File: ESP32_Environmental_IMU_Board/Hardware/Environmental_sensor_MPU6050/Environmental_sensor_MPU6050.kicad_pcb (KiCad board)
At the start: 4 copper layers, 0 parts

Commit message: PCB layout started
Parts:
- added BT1: CH291-1220LF, CH291-1220LF:BAT_CH291-1220LF, F.Cu at (142.9, 93.1)
- added C1: 10uF, Capacitor_SMD:C_0805_2012Metric, F.Cu at (130.3, 65.7)
- added C10: 0.1uF, Capacitor_SMD:C_0603_1608Metric, F.Cu at (123.9, 57.3)
- added C11: 0.1uF, Capacitor_SMD:C_0603_1608Metric, F.Cu at (143.4, 63.6)
- added C12: 1uF, Capacitor_SMD:C_0603_1608Metric, F.Cu at (130.6, 59.3)
- added C13: 10uF, Capacitor_SMD:C_0805_2012Metric, F.Cu at (136.2, 70.3)
- added C14: 0.1uF, Capacitor_SMD:C_0603_1608Metric, F.Cu at (136.0, 68.5)
- added C15: 1uF, Capacitor_SMD:C_0603_1608Metric, F.Cu at (145.0, 81.0)
- added C16: 0.1uF, Capacitor_SMD:C_0603_1608Metric, F.Cu at (144.9, 79.5)
- added C17: 0.1uF, Capacitor_SMD:C_0603_1608Metric, F.Cu at (141.0, 77.0)
- added C2: 0.1uF, Capacitor_SMD:C_0603_1608Metric, F.Cu at (132.1, 65.5)
- added C4: 10uF, Capacitor_SMD:C_0805_2012Metric, F.Cu at (138.1, 65.4)
- added C7: 0.1uF, Capacitor_SMD:C_0603_1608Metric, F.Cu at (139.9, 65.2)
- added C8: 10uF, Capacitor_SMD:C_0805_2012Metric, F.Cu at (145.2, 63.7)
- added C9: 0.1uF, Capacitor_SMD:C_0603_1608Metric, F.Cu at (130.6, 56.2)
- added D1: MBR0520, Diode_SMD:D_SOD-123, F.Cu at (126.8, 65.3)
- added D2: RED_LED, LED_SMD:LED_0201_0603Metric, F.Cu at (133.6, 62.0)
- added D3: RED_LED, LED_SMD:LED_0201_0603Metric, F.Cu at (145.3, 66.7)
- added D4: RED_LED, LED_SMD:LED_0201_0603Metric, F.Cu at (142.0, 67.4)
- added D5: RED_LED, LED_SMD:LED_0201_0603Metric, F.Cu at (145.3, 69.5)
- added FID1: Fiducial, Fiducial:Fiducial_0.75mm_Mask1.5mm, F.Cu at (166.7, 102.7)
- added FID2: Fiducial, Fiducial:Fiducial_0.75mm_Mask1.5mm, F.Cu at (119.8, 56.9)
- added FID3: Fiducial, Fiducial:Fiducial_0.75mm_Mask1.5mm, F.Cu at (120.4, 102.3)
- added J1: Conn_01x04_Pin, Connector_PinHeader_2.54mm:PinHeader_1x04_P2.54mm_Vertical, F.Cu at (168.4, 91.8)
- added J2: Conn_01x04_Pin, Connector_PinHeader_2.54mm:PinHeader_1x04_P2.54mm_Vertical, F.Cu at (124.0, 98.8)
- added J3: USB_C_Receptacle_USB2.0_16P, Connector_USB:USB_C_Receptacle_HCTL_HC-TYPE-C-16P-01A, F.Cu at (119.5, 69.4)
- added J4: Micro_SD_Card, Connector_Card:microSD_HC_Hirose_DM3AT-SF-PEJM5, F.Cu at (126.3, 82.9)
- added R1: 4.7k, Resistor_SMD:R_0603_1608Metric, F.Cu at (164.7, 85.3)
- added R10: 1K, Resistor_SMD:R_0603_1608Metric, F.Cu at (147.6, 69.9)
- added R11: 22, Resistor_SMD:R_0603_1608Metric, F.Cu at (132.6, 69.0)
- added R12: 22, Resistor_SMD:R_0603_1608Metric, F.Cu at (132.6, 70.5)
- added R13: 33, Resistor_SMD:R_0603_1608Metric, F.Cu at (136.7, 83.4)
- added R14: 33, Resistor_SMD:R_0603_1608Metric, F.Cu at (136.7, 79.0)
- added R15: 0, Resistor_SMD:R_0603_1608Metric, F.Cu at (136.7, 77.0)
- added R16: 10k, Resistor_SMD:R_0603_1608Metric, F.Cu at (142.6, 77.0)
- added R17: 33, Resistor_SMD:R_0603_1608Metric, F.Cu at (136.7, 81.2)
- added R2: 4.7k, Resistor_SMD:R_0603_1608Metric, F.Cu at (164.7, 82.8)
- added R3: 0, Resistor_SMD:R_0603_1608Metric, F.Cu at (147.7, 62.7)
- added R4: 10k, Resistor_SMD:R_0603_1608Metric, F.Cu at (147.7, 64.3)
- added R5: 5.1k, Resistor_SMD:R_0603_1608Metric, F.Cu at (125.9, 68.1)
- added R6: 5.1k, Resistor_SMD:R_0603_1608Metric, F.Cu at (125.9, 71.1)
- added R7: 1K, Resistor_SMD:R_0603_1608Metric, F.Cu at (129.8, 61.6)
- added R8: 1K, Resistor_SMD:R_0603_1608Metric, F.Cu at (147.7, 67.1)
- added R9: 1K, Resistor_SMD:R_0603_1608Metric, F.Cu at (142.7, 66.1)
- added SW1: SW_Push, Button_Switch_SMD:SW_Push_SPST_NO_Alps_SKRK, F.Cu at (133.2, 57.5)
- added SW2: SW_Push, Button_Switch_SMD:SW_Push_SPST_NO_Alps_SKRK, F.Cu at (126.4, 57.5)
- added TP3: TP_GND, Test Point:TestPoint_Pad_D2.5mm, F.Cu at (124.6, 93.5)
- added TP6: TP_3V3, Test Point:TestPoint_Pad_D2.5mm, F.Cu at (128.8, 93.5)
- added TP7: TP_TX, Test Point:TestPoint_Pad_D2.5mm, F.Cu at (157.9, 97.1)
- added TP8: TP_RX, Test Point:TestPoint_Pad_D2.5mm, F.Cu at (161.7, 97.0)
- added U2: AP2112K-3.3, Package_TO_SOT_SMD:SOT-23-5, F.Cu at (135.0, 65.5)
- added U3: USBLC6-2P6, Package_TO_SOT_SMD:SOT-666, F.Cu at (129.5, 69.6)
- added U4: ESP32-S3-WROOM-1, RF_Module:ESP32-S3-WROOM-1, F.Cu at (159.0, 66.7)
- added U5: BME280, Package_LGA:Bosch_LGA-8_2.5x2.5mm_P0.65mm_ClockwisePinNumbering, F.Cu at (144.9, 77.1)
- added U6: DS3231M, Package_SO:SOIC-16W_7.5x10.3mm_P1.27mm, F.Cu at (156.9, 87.3)
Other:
- board outline added: 53.5 x 52.1 mm

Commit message: PCB layout started
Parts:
- added C1: 0.1uF, Capacitor_SMD:C_0805_2012Metric, F.Cu at (71.8, 42.4)
- added C12: 100nF, Capacitor_SMD:C_0805_2012Metric, F.Cu at (76.2, 42.4)
- added C13: 22uF/6.3V, Capacitor_SMD:C_0805_2012Metric, F.Cu at (76.2, 45.4)
- added C2: NS, Capacitor_SMD:C_0805_2012Metric, F.Cu at (71.8, 45.4)
- added C22: 100nF, Capacitor_SMD:C_0805_2012Metric, F.Cu at (76.2, 48.4)
- added C23: 100nF, Capacitor_SMD:C_0805_2012Metric, F.Cu at (76.2, 51.4)
- added C24: 1uF, Capacitor_SMD:C_0603_1608Metric, F.Cu at (89.0, 46.7)
- added C25: 0.1uF, Capacitor_SMD:C_0603_1608Metric, F.Cu at (89.0, 49.2)
- added C3: 10uF/50V, Capacitor_SMD:C_0805_2012Metric, F.Cu at (71.8, 48.4)
- added C5: 220pF, Capacitor_SMD:C_0805_2012Metric, F.Cu at (71.8, 51.4)
- added C8: 4.7uF, Capacitor_SMD:C_0805_2012Metric, F.Cu at (71.8, 54.4)
- added CIN1: 10uF, Capacitor_SMD:C_0805_2012Metric, F.Cu at (76.2, 54.4)
- added D2: RED_LED, LED_SMD:LED_0201_0603Metric, F.Cu at (99.5, 36.5)
- added D3: D_Schottky, Diode_SMD:D_SMA, F.Cu at (91.1, 43.1)
- added D4: D, Diode_SMD:D_SOD-123F, F.Cu at (97.8, 53.1)
- added D5: D, Diode_SMD:D_SOD-123F, F.Cu at (97.8, 56.5)
- added IC1: MP1584EN-LF-Z, MP1584EN-LF-Z:SOIC127P600X170-9N, F.Cu at (82.7, 52.7)
- added J2: Conn_01x02, Connector_JST:JST_PH_B2B-PH-K_1x02_P2.00mm_Vertical, F.Cu at (95.9, 31.8)
- added L1: 10uH, Inductor_SMD:L_6.3x6.3_H3, F.Cu at (82.7, 44.8)
- added R12: 4.7k, Resistor_SMD:R_0603_1608Metric, F.Cu at (93.0, 49.2)
- added R13: 4.7k, Resistor_SMD:R_0603_1608Metric, F.Cu at (93.0, 51.7)
- added R5: 200k, Resistor_SMD:R_0603_1608Metric, F.Cu at (89.0, 56.7)
- added R8: 40k, Resistor_SMD:R_0603_1608Metric, F.Cu at (89.0, 59.2)
- added R9: 124k, Resistor_SMD:R_0603_1608Metric, F.Cu at (93.0, 46.7)
- added R_LED1: 1K, Resistor_SMD:R_0603_1608Metric, F.Cu at (93.0, 54.2)
- added R_PRG1: 1K, Resistor_SMD:R_0603_1608Metric, F.Cu at (93.0, 56.7)
- added U1: MCP73831-2-OT, Package_TO_SOT_SMD:SOT-23-5, F.Cu at (95.5, 38.0)
- added U10: MLX90614ESF-BAA-000-TU, MLX90614ESF-BAA-000-TU:TO254P942H425-4, F.Cu at (87.6, 34.4)
- added U6: SCD40-D-R2, Sensor:Sensirion_SCD4x-1EP_10.1x10.1mm_P1.25mm_EP4.8x4.8mm, F.Cu at (75.8, 35.0)
- added U8: ENS160-BGLM, ENS160-BGLM:XDCR_ENS160-BGLM, F.Cu at (98.0, 48.4)
- added U9: OPT3001IDNPRQ1, OPT3001IDNPRQ1:SON65P200X200X65-7N, F.Cu at (97.7, 42.6)
- R1: value 4.7k -> 68.1k
- R2: value 4.7k -> 100k
- moved R1 82.9 mm to (89.0, 51.7), turned to 0 degrees
- moved R2 81.0 mm to (89.0, 54.2), turned to 0 degrees
- renumbered C4 to C10, C7 to C11, C8 to C14, C11 to C15, C9 to C16, C10 to C17, C12 to C18, C15 to C19, C16 to C20, C17 to C21, C1 to C4, C2 to C6, C13 to C7, C14 to C9, D2 to D6, D3 to D7, D4 to D8, D5 to D9, J3 to J1, J2 to J3, J1 to J4, J4 to J5, R3 to R10, R4 to R11, R16 to R14, R13 to R15, R17 to R16, R14 to R17, R15 to R18, R5 to R3, R6 to R4, R11 to R6, R12 to R7, R7 to R_LED2, R8 to R_LED3, R9 to R_LED4, R10 to R_LED5, TP3 to TP1, TP6 to TP2, TP7 to TP3, TP8 to TP4, U5 to U4, U4 to U5, U6 to U7
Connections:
- J4 pad 3: Net-(J1-Pin_3) -> SCL/IO9
- J4 pad 4: Net-(J1-Pin_4) -> SDA/IO8
- R1 pad 1: Net-(J1-Pin_3) -> GND
- R1 pad 2: SCL/IO9 -> Net-(C5-Pad2)
- R10 pad 2: ESP32_3V3 -> Net-(D5-A)
- R2 pad 1: Net-(J1-Pin_4) -> BAT+
- R2 pad 2: SDA/IO8 -> BAT+
- TP2 pad 1: ESP32_3V3 -> Net-(D5-A)
- U5 pad 12: SDA/IO8 -> Net-(U5-IO8)
- U5 pad 17: SCL/IO9 -> Net-(U5-IO9)
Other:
- board outline removed

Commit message: PCB Layout done
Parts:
- moved U6 80.1 mm to (134.2, 89.8), turned to 180 degrees
- moved U10 75.5 mm to (124.6, 100.2), turned to -90 degrees
- moved J4 73.6 mm to (95.7, 102.8), turned to 90 degrees
- moved C24 70.6 mm to (130.0, 104.2)
- moved R11 69.7 mm to (79.2, 51.7), turned to -90 degrees
- moved C25 67.0 mm to (130.9, 101.5), turned to -90 degrees
- moved C22 65.3 mm to (115.1, 100.8)
- moved SW1 57.9 mm to (75.3, 54.6), turned to 0 degrees
- moved TP2 57.2 mm to (89.0, 52.4), turned to 90 degrees
- moved TP1 56.8 mm to (85.3, 52.4)
- moved C23 55.6 mm to (109.7, 95.8), turned to 90 degrees
- moved C7 55.6 mm to (82.0, 58.1), turned to -90 degrees
- moved FID1 55.5 mm to (137.2, 55.6)
- moved C16 55.0 mm to (75.7, 52.0), turned to 0 degrees
- moved U8 54.9 mm to (110.8, 101.8)
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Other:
- board outline added: 72.9 x 58.4 mm
- board text added: "+"
- board text added: "-"
- board text added: "BAT_IN"
- board text added: "BOOT"
- board text added: "EN"
- board text added: "I2C CONNECTOR"
- board text added: "Indoor Environmental Quality (IEQ) Auditor"
- board text added: "OLED DISPLAY"
- board text added: "POWER SECTION"
- board text added: "RX"
- board text added: "SD CARD"
- board text added: "TX"

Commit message: PCB Layout modified
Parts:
- moved J4 2.61 mm to (94.3, 100.5)
- moved J3 2.13 mm to (135.6, 80.3)
- moved FID2 0.80 mm to (137.1, 99.3)
- moved FID3 0.30 mm to (71.0, 99.3)
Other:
- board text added: "3V3"
- board text added: "GND"
- board text added: "OLED"
- board text added: "SCL"
- board text added: "SDA"
- board text removed: "OLED DISPLAY"
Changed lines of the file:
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@@
 		(capping no)
 		(filling no)
-		(zone_defaults)
 		(pcbplotparams
 			(layerselection 0x00000000_00000000_55555555_5755f5ff)
@@
 	(footprint "Fiducial:Fiducial_0.75mm_Mask1.5mm"
 		(layer "F.Cu")
-		(at 70.975 99.6)
+		(at 71.025 99.3)
 		(descr "Fiducial, circular marking, 0.75mm bare copper, 1.5mm soldermask opening (Level B)")
 		(tags "fiducial")
@@
 	(footprint "Connector_PinHeader_2.54mm:PinHeader_1x04_P2.54mm_Vertical"
 		(layer "F.Cu")
-		(at 95.67 102.75 90)
+		(at 94.265 100.55 90)
 		(descr "Through hole straight pin header, 1x04, 2.54mm pitch, single row")
 		(tags "Through hole pin header THT 1x04 2.54mm single row")
@@
 	(footprint "Fiducial:Fiducial_0.75mm_Mask1.5mm"
 		(layer "F.Cu")
-		(at 137 98.5)
+		(at 137.05 99.3)
 		(descr "Fiducial, circular marking, 0.75mm bare copper, 1.5mm soldermask opening (Level B)")
 		(tags "fiducial")
@@
 	(footprint "Connector_PinHeader_2.54mm:PinHeader_1x04_P2.54mm_Vertical"
 		(layer "F.Cu")
-		(at 137.35 81.45 180)
+		(at 135.575 80.275 180)
 		(descr "Through hole straight pin header, 1x04, 2.54mm pitch, single row")
 		(tags "Through hole pin header THT 1x04 2.54mm single row")
@@
 	)
 	(gr_text "I2C CONNECTOR"
-		(at 93.55 100.25 0)
+		(at 92.145 98.05 0)
 		(layer "F.SilkS" knockout)
 		(effects
@@
 		)
 	)
+	(gr_text "GND"
+		(at 137.6 80.8 0)
+		(layer "F.SilkS")
+		(effects
+			(font
+				(size 0.8 1)
+				(thickness 0.15)
+			)
+			(justify left bottom)
+		)
+	)
+	(gr_text "SCL"
+		(at 137.7 75.725 0)
+		(layer "F.SilkS")
+		(effects
+			(font
+				(size 0.8 1)
+				(thickness 0.15)
+			)
+			(justify left bottom)
+		)
+	)
+	(gr_text "3V3"
+		(at 137.7 78.35 0)
+		(layer "F.SilkS")
+		(effects
+			(font
+				(size 0.8 1)
+				(thickness 0.15)
+			)
+			(justify left bottom)
+		)
+	)
+	(gr_text "SDA"
+		(at 137.725 73.05 0)
+		(layer "F.SilkS")
+		(effects
+			(font
+				(size 0.8 1)
+				(thickness 0.15)
+			)
+			(justify left bottom)
+		)
+	)
 	(gr_text "BAT_IN"
 		(at 69.9 80.025 90)
@@
 		)
 	)
-	(gr_text "OLED DISPLAY"
-		(at 134.65 83.1 90)
+	(gr_text "GND\n"
+		(at 94.825 105.65 90)
+		(layer "F.SilkS")
+		(effects
+			(font
+				(size 0.8 1)
+				(thickness 0.15)
+			)
+			(justify left bottom)
+		)
+	)
+	(gr_text "3V3"
+		(at 97.275 105.55 90)
+		(layer "F.SilkS")
+		(effects
+			(font
+				(size 0.8 1)
+				(thickness 0.15)
+			)
+			(justify left bottom)
+		)
+	)
+	(gr_text "SCL"
+		(at 99.775 105.525 90)
+		(layer "F.SilkS")
+		(effects
+			(font
+				(size 0.8 1)
+				(thickness 0.15)
+			)
+			(justify left bottom)
+		)
+	)
+	(gr_text "SDA"
+		(at 102.325 105.525 90)
+		(layer "F.SilkS")
+		(effects
+			(font
+				(size 0.8 1)
+				(thickness 0.15)
+			)
+			(justify left bottom)
+		)
+	)
+	(gr_text "OLED"
+		(at 132.825 81.8 90)
 		(layer "F.SilkS" knockout)
 		(effects

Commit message: DRC Errors resolved
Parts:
- moved R14 22.2 mm to (124.2, 101.8)
- moved C19 22.2 mm to (119.4, 103.1)
- moved C20 22.2 mm to (117.9, 103.2)
- moved U4 22.2 mm to (121.9, 102.3)
- moved C22 18.8 mm to (133.9, 101.2)
- moved U8 18.8 mm to (129.6, 102.2)
- moved C24 15.7 mm to (114.5, 102.0)
- moved C25 15.7 mm to (115.4, 99.3)
- moved U10 15.7 mm to (109.1, 98.0)
- moved C23 10.1 mm to (100.9, 90.9), turned to 180 degrees
- moved U9 5.57 mm to (101.0, 94.2), turned to -90 degrees
- moved D9 0.10 mm to (111.5, 68.5)

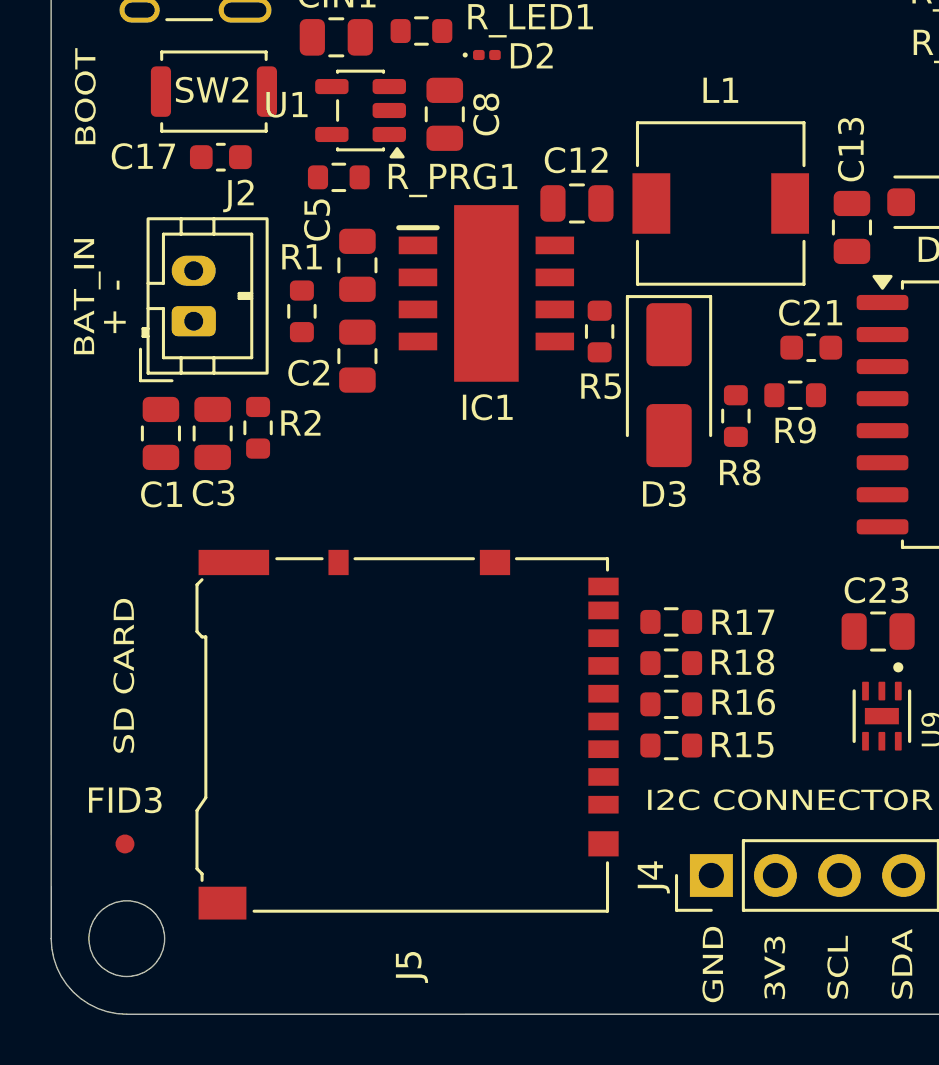
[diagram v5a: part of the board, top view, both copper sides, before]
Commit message: Battery footprint changed
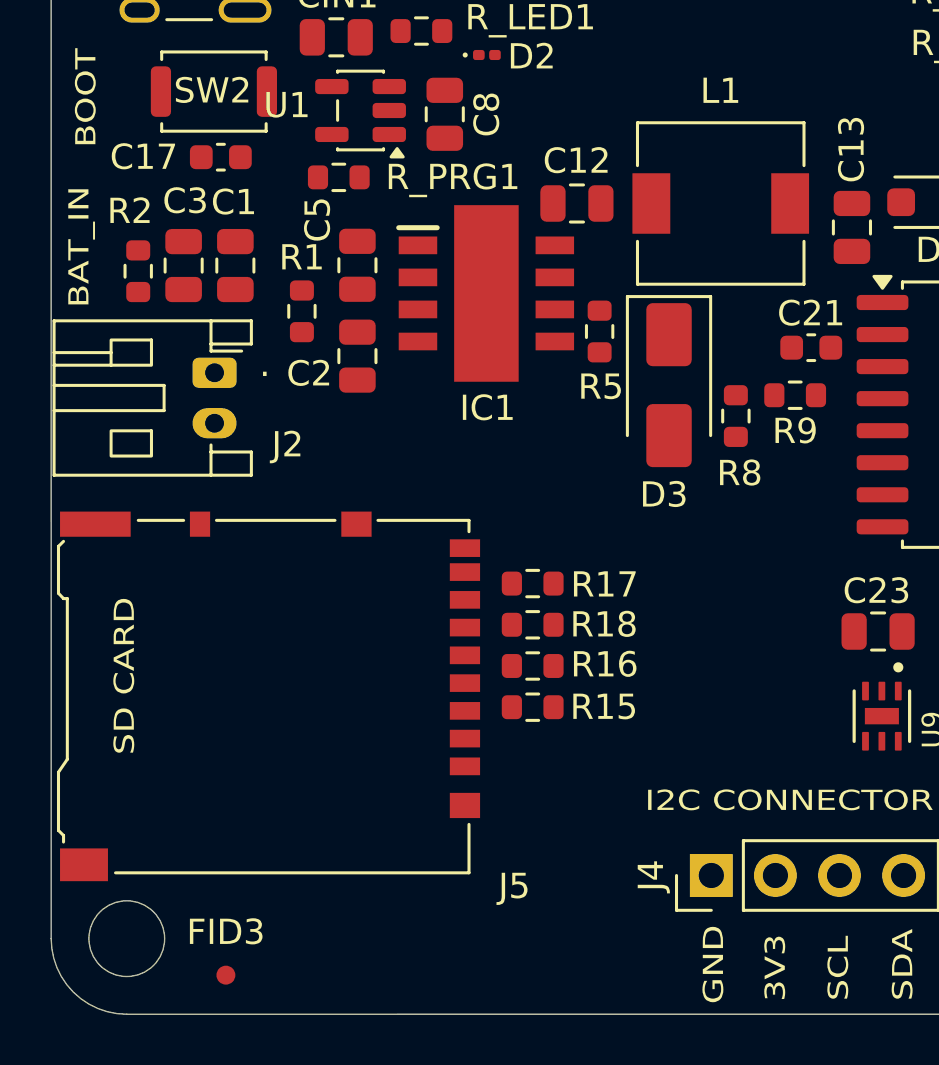
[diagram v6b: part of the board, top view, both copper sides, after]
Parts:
- J2: footprint Connector_JST:JST_PH_B2B-PH-K_1x02_P2.00mm_Vertical -> Connector_JST:JST_PH_S2B-PH-K_1x02_P2.00mm_Horizontal
- moved R2 7.81 mm to (71.5, 76.6), turned to 90 degrees
- moved C1 7.28 mm to (75.4, 76.4), turned to 90 degrees
- moved C3 6.75 mm to (73.3, 76.4), turned to 90 degrees
- moved FID3 6.56 mm to (75.0, 104.5)
- moved R15 5.70 mm to (87.2, 93.9)
- moved J5 5.70 mm to (76.8, 93.5)
- moved R16 5.70 mm to (87.2, 92.2)
- moved R17 5.70 mm to (87.2, 89.0)
- moved R18 5.70 mm to (87.2, 90.6)
- moved J2 2.21 mm to (74.6, 80.6), turned to -90 degrees
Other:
- board text added: "."
- board text removed: "+"
- board text removed: "-"

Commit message: Routing strted
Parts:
- moved J4 2.26 mm to (92.0, 100.6)
- moved R7 1.04 mm to (86.3, 62.1)
- moved R6 1.02 mm to (86.3, 60.6)
- moved U3 0.84 mm to (82.8, 61.4)
- moved R3 0.56 mm to (79.2, 60.1)
- moved C24 0.46 mm to (114.1, 102.1)
- moved C25 0.46 mm to (115.0, 99.4)
- moved U10 0.46 mm to (108.7, 98.2)
- turned D6 to 180 degrees
- turned D7 to 180 degrees
- turned D8 to 180 degrees
- turned D9 to 180 degrees
- turned R16 to 180 degrees
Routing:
- net GND: track 0.00 -> 263.7 mm, vias 0 -> 3
- net ESP32_3V3: track 0.00 -> 177.6 mm, vias 0 -> 4
- net SCL/IO9: track 0.00 -> 70.3 mm, vias 0 -> 2
- net MISO: track 0.00 -> 49.2 mm
- net CHIP-PU/RST/EN: track 0.00 -> 47.3 mm, vias 0 -> 2
- net SDA/IO8: track 0.00 -> 41.7 mm, vias 0 -> 1
- net USB_D+: track 0.00 -> 31.4 mm
- net USB_D-: track 0.00 -> 31.1 mm
- net Net-(D5-A): track 0.00 -> 22.8 mm
- net Net-(D3-K): track 0.00 -> 16.7 mm
- net Net-(U7-VBAT): track 0.00 -> 10.5 mm
- net ERR_LED: track 0.00 -> 9.84 mm, vias 0 -> 2
- net Net-(J5-SHIELD): track 0.00 -> 9.53 mm, vias 0 -> 2
- net BAT+: track 0.00 -> 9.18 mm
- net Net-(U5-RXD0): track 0.00 -> 8.51 mm
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- added copper zone on In1.Cu, net GND

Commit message: PCB Layout modified
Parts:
- moved U7 20.6 mm to (95.8, 64.2)
- moved C15 5.30 mm to (104.2, 53.4), turned to 90 degrees
- moved C14 5.30 mm to (102.4, 53.5), turned to 90 degrees
- moved R10 5.30 mm to (106.6, 52.7)
- moved D5 4.68 mm to (110.4, 52.2)
- moved R13 4.57 mm to (117.5, 70.5)
- moved U5 4.55 mm to (122.8, 56.1)
- moved BT1 4.47 mm to (120.7, 81.5)
- moved D8 4.46 mm to (111.2, 62.1)
- moved D9 4.46 mm to (111.2, 64.1)
- moved R12 4.46 mm to (111.1, 65.2)
- moved R_LED2 4.46 mm to (108.6, 56.8)
- moved R_LED3 4.46 mm to (108.7, 58.9)
- moved R_LED5 4.46 mm to (108.7, 63.1)
- moved D6 4.46 mm to (111.3, 57.9)
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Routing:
- net GND: track 263.7 -> 0.00 mm, vias 3 -> 0
- net ESP32_3V3: track 177.6 -> 0.00 mm, vias 4 -> 0
- net SCL/IO9: track 70.3 -> 0.00 mm, vias 2 -> 0
- net MISO: track 49.2 -> 0.00 mm
- net CHIP-PU/RST/EN: track 47.3 -> 0.00 mm, vias 2 -> 0
- net SDA/IO8: track 41.7 -> 0.00 mm, vias 1 -> 0
- net USB_D+: track 31.4 -> 0.00 mm
- net USB_D-: track 31.1 -> 0.00 mm
- net Net-(D5-A): track 22.8 -> 0.00 mm
- net Net-(D3-K): track 16.7 -> 0.00 mm
- net Net-(U7-VBAT): track 10.5 -> 0.00 mm
- net ERR_LED: track 9.84 -> 0.00 mm, vias 2 -> 0
- net Net-(J5-SHIELD): track 9.53 -> 0.00 mm, vias 2 -> 0
- net BAT+: track 9.18 -> 0.00 mm
- net Net-(U5-RXD0): track 8.51 -> 0.00 mm
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- removed copper zone on In1.Cu, net GND
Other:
- board size 72.9 x 58.4 mm -> 72.9 x 62.9 mm
- board text removed: "Indoor Environmental Quality (IEQ) Auditor"
